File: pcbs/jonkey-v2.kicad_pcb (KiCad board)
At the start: 2 copper layers, 191.3 x 127.7 mm, 149 parts

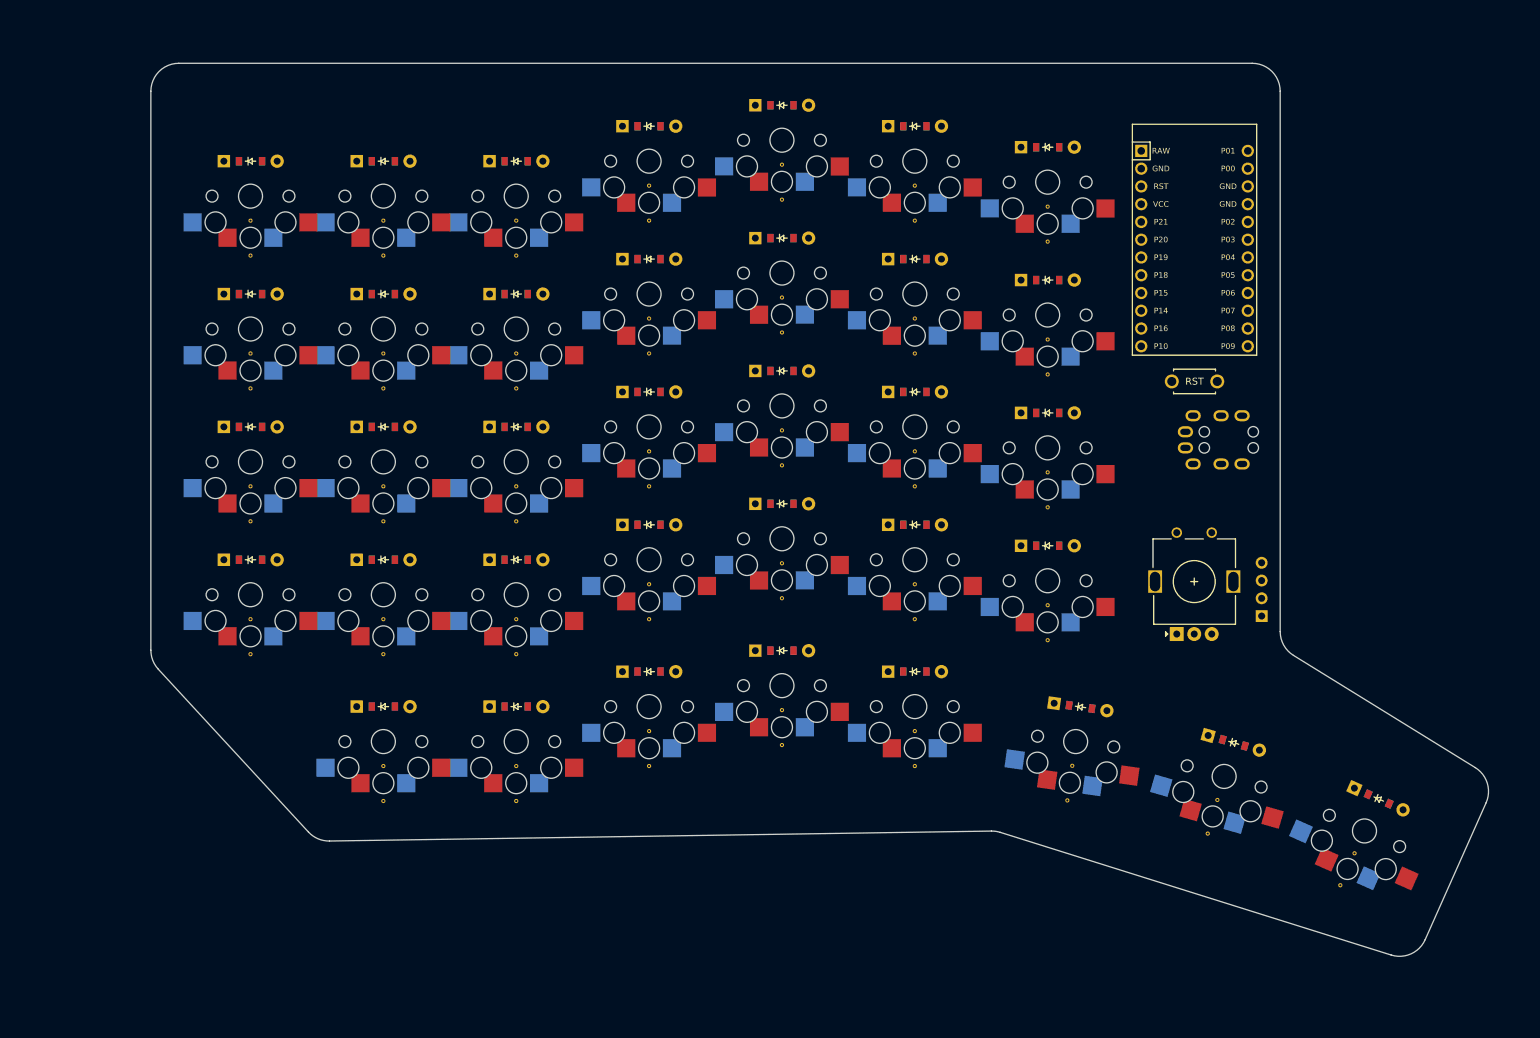
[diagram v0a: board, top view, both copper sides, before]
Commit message: feat: add a few mounting holds, increase thumb distance, increase stagger beyound pinky
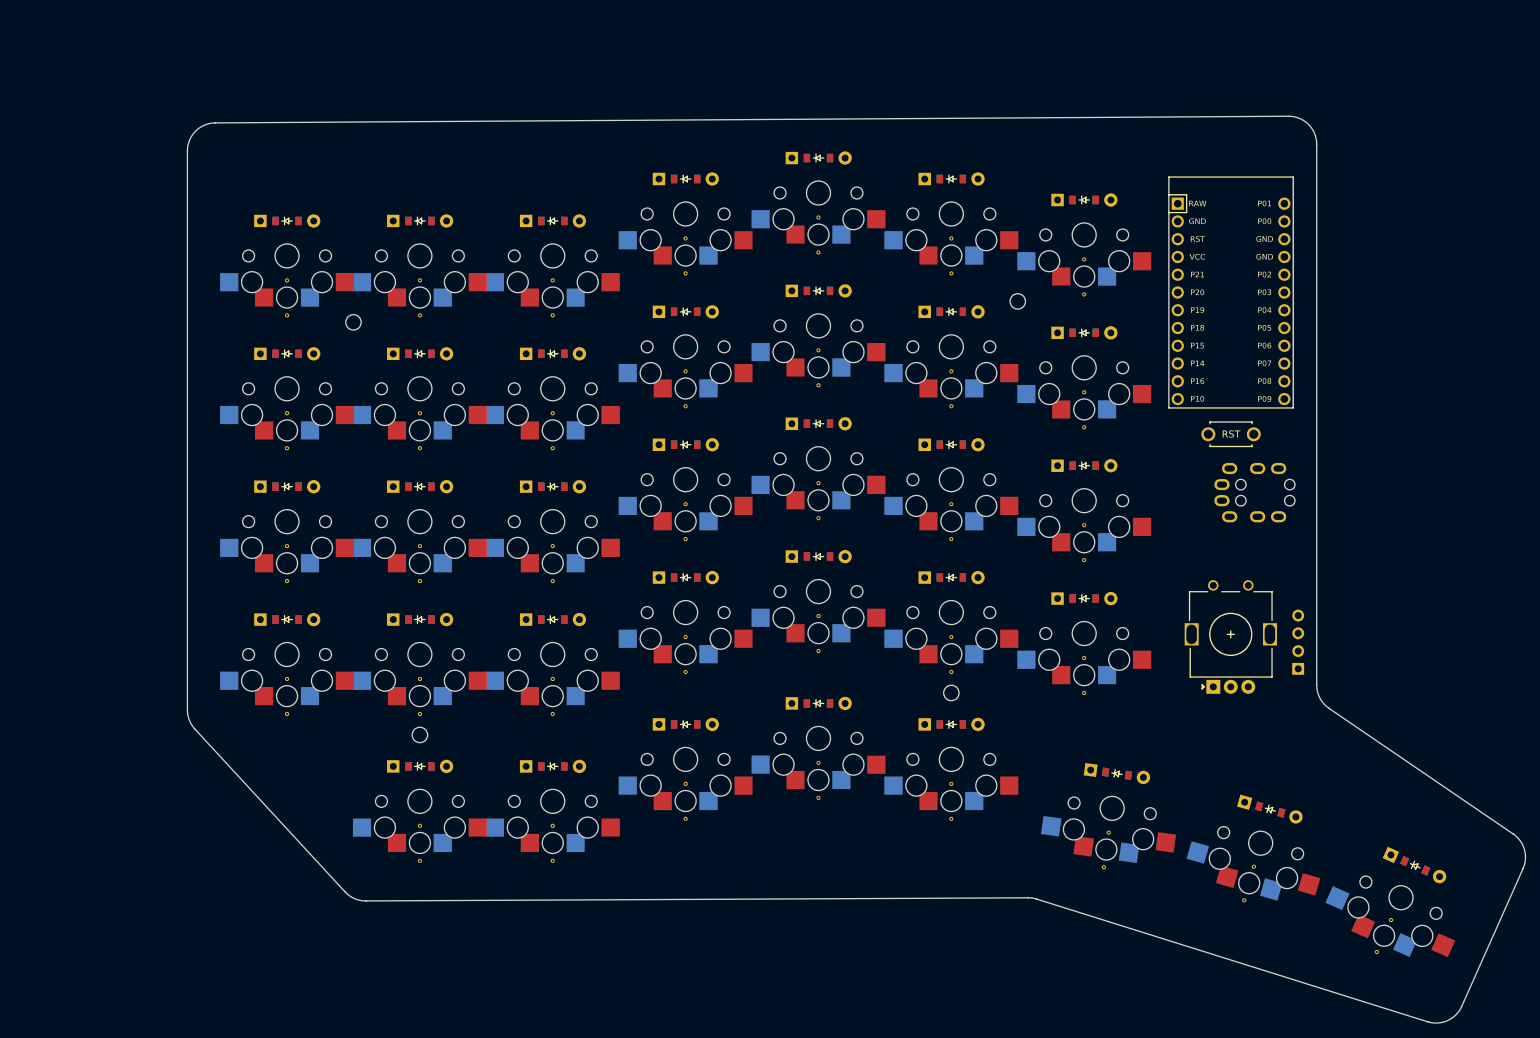
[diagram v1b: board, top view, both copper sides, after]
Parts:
- removed the REF** at (184.0, 158.0)
- removed the REF** at (165.0, 189.0)
- removed the REF** at (244.5, 184.0)
- removed the REF** at (241.0, 109.0)
- removed the REF** at (165.0, 149.0)
- removed the REF** at (127.0, 168.0)
- removed the REF** at (184.0, 125.0)
- removed the REF** at (184.0, 106.0)
- removed the REF** at (127.0, 144.0)
- removed the REF** at (222.0, 158.0)
- removed the REF** at (222.0, 106.0)
- removed the REF** at (146.0, 184.0)
- removed the REF** at (203.0, 122.0)
- removed the REF** at (184.0, 139.0)
- removed the REF** at (222.0, 120.0)
- removed the REF** at (203.0, 136.0)
- removed the REF** at (222.0, 184.0)
- removed the REF** at (165.0, 111.0)
- removed the REF** at (241.0, 128.0)
- removed the REF** at (165.0, 125.0)
- removed the REF** at (146.0, 106.0)
- removed the REF** at (222.0, 144.0)
- removed the REF** at (243.8, 188.9)
- removed the REF** at (203.0, 155.0)
- removed the REF** at (127.0, 111.0)
- removed the REF** at (222.0, 179.0)
- removed the REF** at (165.0, 106.0)
- removed the REF** at (165.0, 163.0)
- removed the REF** at (146.0, 125.0)
- removed the REF** at (127.0, 125.0)
- removed the REF** at (146.0, 163.0)
- removed the REF** at (241.0, 166.0)
- removed the REF** at (203.0, 98.0)
- removed the REF** at (127.0, 163.0)
- removed the REF** at (284.9, 196.5)
- removed the REF** at (222.0, 101.0)
- removed the REF** at (222.0, 163.0)
- removed the REF** at (165.0, 144.0)
- removed the REF** at (241.0, 123.0)
- removed the REF** at (146.0, 149.0)
- removed the REF** at (282.8, 201.0)
- removed the REF** at (241.0, 147.0)
- removed the REF** at (203.0, 141.0)
- removed the REF** at (146.0, 144.0)
- removed the REF** at (165.0, 168.0)
- removed the REF** at (184.0, 101.0)
- removed the REF** at (146.0, 189.0)
- removed the REF** at (146.0, 130.0)
- removed the REF** at (165.0, 184.0)
- removed the REF** at (165.0, 130.0)
- removed the REF** at (184.0, 120.0)
- removed the REF** at (222.0, 125.0)
- removed the REF** at (265.3, 188.8)
- removed the REF** at (127.0, 149.0)
- removed the REF** at (146.0, 168.0)
- removed the REF** at (263.9, 193.7)
- removed the REF** at (184.0, 179.0)
- removed the REF** at (184.0, 144.0)
- removed the REF** at (127.0, 130.0)
- removed the REF** at (241.0, 104.0)
- removed the REF** at (241.0, 161.0)
- removed the REF** at (127.0, 106.0)
- removed the REF** at (184.0, 163.0)
- removed the REF** at (203.0, 103.0)
- removed the REF** at (184.0, 184.0)
- removed the REF** at (203.0, 117.0)
- removed the REF** at (146.0, 111.0)
- removed the REF** at (222.0, 139.0)
- removed the REF** at (203.0, 181.0)
- removed the REF** at (203.0, 176.0)
- removed the REF** at (241.0, 142.0)
- removed the REF** at (203.0, 160.0)
- added MH1: , ceoloide:mounting_hole_npth, F.Cu at (141.7, 120.5)
- added MH2: , ceoloide:mounting_hole_npth, F.Cu at (236.7, 117.5)
- added MH3: , ceoloide:mounting_hole_npth, F.Cu at (151.2, 179.6)
- added MH4: , ceoloide:mounting_hole_npth, F.Cu at (227.2, 173.6)
- added REF**: VIA-0.6mm, VIA-0.6mm, F.Cu at (170.2, 197.6)
- added REF**: VIA-0.6mm, VIA-0.6mm, F.Cu at (189.2, 146.6)
- added REF**: VIA-0.6mm, VIA-0.6mm, F.Cu at (246.2, 173.6)
- added REF**: VIA-0.6mm, VIA-0.6mm, F.Cu at (227.2, 191.6)
- added REF**: VIA-0.6mm, VIA-0.6mm, F.Cu at (151.2, 176.6)
- added REF**: VIA-0.6mm, VIA-0.6mm, F.Cu at (189.2, 127.5)
- added REF**: VIA-0.6mm, VIA-0.6mm, F.Cu at (132.2, 152.6)
- added REF**: VIA-0.6mm, VIA-0.6mm, F.Cu at (189.2, 108.5)
- added REF**: VIA-0.6mm, VIA-0.6mm, F.Cu at (170.2, 119.5)
- added REF**: VIA-0.6mm, VIA-0.6mm, F.Cu at (132.2, 176.6)
- added REF**: VIA-0.6mm, VIA-0.6mm, F.Cu at (170.2, 157.6)
- added REF**: VIA-0.6mm, VIA-0.6mm, F.Cu at (246.2, 168.6)
- added REF**: VIA-0.6mm, VIA-0.6mm, F.Cu at (132.2, 171.6)
- added REF**: VIA-0.6mm, VIA-0.6mm, F.Cu at (151.2, 192.6)
- added REF**: VIA-0.6mm, VIA-0.6mm, F.Cu at (249.7, 193.5)
- added REF**: VIA-0.6mm, VIA-0.6mm, F.Cu at (208.2, 162.6)
- added REF**: VIA-0.6mm, VIA-0.6mm, F.Cu at (132.2, 114.5)
- added REF**: VIA-0.6mm, VIA-0.6mm, F.Cu at (246.2, 111.5)
- added REF**: VIA-0.6mm, VIA-0.6mm, F.Cu at (189.2, 113.5)
- added REF**: VIA-0.6mm, VIA-0.6mm, F.Cu at (208.2, 148.6)
- added REF**: VIA-0.6mm, VIA-0.6mm, F.Cu at (227.2, 132.6)
- added REF**: VIA-0.6mm, VIA-0.6mm, F.Cu at (227.2, 151.6)
- added REF**: VIA-0.6mm, VIA-0.6mm, F.Cu at (227.2, 165.6)
- added REF**: VIA-0.6mm, VIA-0.6mm, F.Cu at (246.2, 149.6)
- added REF**: VIA-0.6mm, VIA-0.6mm, F.Cu at (208.2, 124.5)
- added REF**: VIA-0.6mm, VIA-0.6mm, F.Cu at (208.2, 183.6)
- added REF**: VIA-0.6mm, VIA-0.6mm, F.Cu at (170.2, 176.6)
- added REF**: VIA-0.6mm, VIA-0.6mm, F.Cu at (170.2, 192.6)
- added REF**: VIA-0.6mm, VIA-0.6mm, F.Cu at (189.2, 186.6)
- added REF**: VIA-0.6mm, VIA-0.6mm, F.Cu at (189.2, 170.6)
- added REF**: VIA-0.6mm, VIA-0.6mm, F.Cu at (208.2, 110.5)
- added REF**: VIA-0.6mm, VIA-0.6mm, F.Cu at (227.2, 186.6)
- added REF**: VIA-0.6mm, VIA-0.6mm, F.Cu at (246.2, 154.6)
- added REF**: VIA-0.6mm, VIA-0.6mm, F.Cu at (288.1, 210.6)
- added REF**: VIA-0.6mm, VIA-0.6mm, F.Cu at (208.2, 129.6)
- added REF**: VIA-0.6mm, VIA-0.6mm, F.Cu at (208.2, 188.6)
- added REF**: VIA-0.6mm, VIA-0.6mm, F.Cu at (132.2, 133.6)
- added REF**: VIA-0.6mm, VIA-0.6mm, F.Cu at (227.2, 146.6)
- added REF**: VIA-0.6mm, VIA-0.6mm, F.Cu at (227.2, 113.5)
- added REF**: VIA-0.6mm, VIA-0.6mm, F.Cu at (132.2, 119.5)
- added REF**: VIA-0.6mm, VIA-0.6mm, F.Cu at (170.2, 114.5)
- added REF**: VIA-0.6mm, VIA-0.6mm, F.Cu at (246.2, 130.6)
- added REF**: VIA-0.6mm, VIA-0.6mm, F.Cu at (170.2, 138.6)
- added REF**: VIA-0.6mm, VIA-0.6mm, F.Cu at (227.2, 108.5)
- added REF**: VIA-0.6mm, VIA-0.6mm, F.Cu at (170.2, 152.6)
- added REF**: VIA-0.6mm, VIA-0.6mm, F.Cu at (132.2, 157.6)
- added REF**: VIA-0.6mm, VIA-0.6mm, F.Cu at (132.2, 138.6)
- added REF**: VIA-0.6mm, VIA-0.6mm, F.Cu at (151.2, 197.6)
- added REF**: VIA-0.6mm, VIA-0.6mm, F.Cu at (227.2, 170.6)
- added REF**: VIA-0.6mm, VIA-0.6mm, F.Cu at (189.2, 151.6)
- added REF**: VIA-0.6mm, VIA-0.6mm, F.Cu at (151.2, 119.5)
- added REF**: VIA-0.6mm, VIA-0.6mm, F.Cu at (151.2, 157.6)
- added REF**: VIA-0.6mm, VIA-0.6mm, F.Cu at (189.2, 165.6)
- added REF**: VIA-0.6mm, VIA-0.6mm, F.Cu at (270.5, 198.4)
- added REF**: VIA-0.6mm, VIA-0.6mm, F.Cu at (151.2, 114.5)
- added REF**: VIA-0.6mm, VIA-0.6mm, F.Cu at (208.2, 143.6)
- added REF**: VIA-0.6mm, VIA-0.6mm, F.Cu at (151.2, 138.6)
- added REF**: VIA-0.6mm, VIA-0.6mm, F.Cu at (269.1, 203.2)
- added REF**: VIA-0.6mm, VIA-0.6mm, F.Cu at (227.2, 127.5)
- added REF**: VIA-0.6mm, VIA-0.6mm, F.Cu at (170.2, 133.6)
- added REF**: VIA-0.6mm, VIA-0.6mm, F.Cu at (189.2, 191.6)
- added REF**: VIA-0.6mm, VIA-0.6mm, F.Cu at (151.2, 171.6)
- added REF**: VIA-0.6mm, VIA-0.6mm, F.Cu at (246.2, 116.5)
- added REF**: VIA-0.6mm, VIA-0.6mm, F.Cu at (170.2, 171.6)
- added REF**: VIA-0.6mm, VIA-0.6mm, F.Cu at (189.2, 132.6)
- added REF**: VIA-0.6mm, VIA-0.6mm, F.Cu at (151.2, 133.6)
- added REF**: VIA-0.6mm, VIA-0.6mm, F.Cu at (208.2, 105.5)
- added REF**: VIA-0.6mm, VIA-0.6mm, F.Cu at (246.2, 135.6)
- added REF**: VIA-0.6mm, VIA-0.6mm, F.Cu at (208.2, 167.6)
- added REF**: VIA-0.6mm, VIA-0.6mm, F.Cu at (151.2, 152.6)
- added REF**: VIA-0.6mm, VIA-0.6mm, F.Cu at (249.0, 198.5)
- added REF**: VIA-0.6mm, VIA-0.6mm, F.Cu at (290.1, 206.0)
- moved S35 10.9 mm to (271.5, 195.0)
- moved S34 10.9 mm to (250.2, 190.1)
- moved D35 10.9 mm to (272.8, 190.2)
- moved S36 10.9 mm to (291.5, 202.8)
- moved D34 10.9 mm to (250.9, 185.1)
- moved D36 10.9 mm to (293.6, 198.3)
- moved D1 10.0 mm to (132.2, 163.1)
- moved D10 10.0 mm to (170.2, 184.1)
- moved D11 10.0 mm to (170.2, 163.1)
- moved D12 10.0 mm to (170.2, 144.1)
- moved D2 10.0 mm to (132.2, 144.1)
- moved D5 10.0 mm to (151.2, 184.1)
- moved D6 10.0 mm to (151.2, 163.1)
- moved D7 10.0 mm to (151.2, 144.1)
- moved S1 10.0 mm to (132.2, 168.1)
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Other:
- board size 191.3 x 127.7 mm -> 191.4 x 129.7 mm

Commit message: feat: add place for pull up resistors for i2c
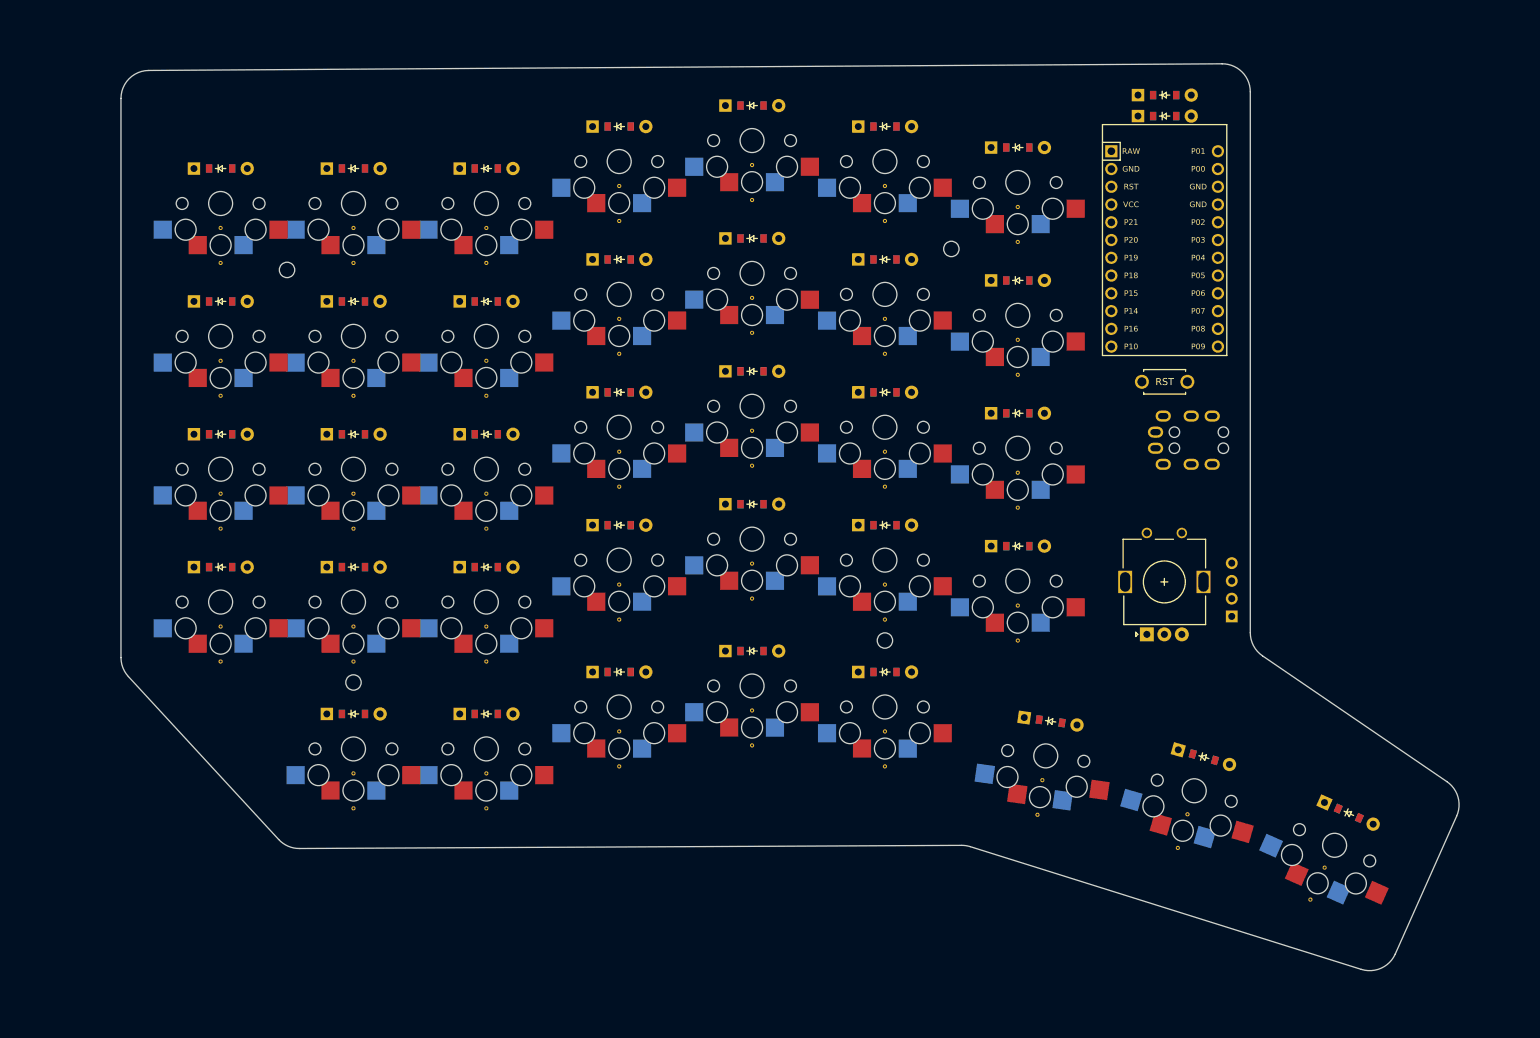
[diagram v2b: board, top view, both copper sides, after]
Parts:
- removed the REF** at (170.2, 197.6)
- removed the REF** at (189.2, 146.6)
- removed the REF** at (246.2, 173.6)
- removed the REF** at (227.2, 191.6)
- removed the REF** at (151.2, 176.6)
- removed the REF** at (189.2, 127.5)
- removed the REF** at (132.2, 152.6)
- removed the REF** at (189.2, 108.5)
- removed the REF** at (170.2, 119.5)
- removed the REF** at (132.2, 176.6)
- removed the REF** at (170.2, 157.6)
- removed the REF** at (246.2, 168.6)
- removed the REF** at (132.2, 171.6)
- removed the REF** at (151.2, 192.6)
- removed the REF** at (249.7, 193.5)
- removed the REF** at (208.2, 162.6)
- removed the REF** at (132.2, 114.5)
- removed the REF** at (246.2, 111.5)
- removed the REF** at (189.2, 113.5)
- removed the REF** at (208.2, 148.6)
- removed the REF** at (227.2, 132.6)
- removed the REF** at (227.2, 151.6)
- removed the REF** at (227.2, 165.6)
- removed the REF** at (246.2, 149.6)
- removed the REF** at (208.2, 124.5)
- removed the REF** at (208.2, 183.6)
- removed the REF** at (170.2, 176.6)
- removed the REF** at (170.2, 192.6)
- removed the REF** at (189.2, 186.6)
- removed the REF** at (189.2, 170.6)
- removed the REF** at (208.2, 110.5)
- removed the REF** at (227.2, 186.6)
- removed the REF** at (246.2, 154.6)
- removed the REF** at (288.1, 210.6)
- removed the REF** at (208.2, 129.6)
- removed the REF** at (208.2, 188.6)
- removed the REF** at (132.2, 133.6)
- removed the REF** at (227.2, 146.6)
- removed the REF** at (227.2, 113.5)
- removed the REF** at (132.2, 119.5)
- removed the REF** at (170.2, 114.5)
- removed the REF** at (246.2, 130.6)
- removed the REF** at (170.2, 138.6)
- removed the REF** at (227.2, 108.5)
- removed the REF** at (170.2, 152.6)
- removed the REF** at (132.2, 157.6)
- removed the REF** at (132.2, 138.6)
- removed the REF** at (151.2, 197.6)
- removed the REF** at (227.2, 170.6)
- removed the REF** at (189.2, 151.6)
- removed the REF** at (151.2, 119.5)
- removed the REF** at (151.2, 157.6)
- removed the REF** at (189.2, 165.6)
- removed the REF** at (270.5, 198.4)
- removed the REF** at (151.2, 114.5)
- removed the REF** at (208.2, 143.6)
- removed the REF** at (151.2, 138.6)
- removed the REF** at (269.1, 203.2)
- removed the REF** at (227.2, 127.5)
- removed the REF** at (170.2, 133.6)
- removed the REF** at (189.2, 191.6)
- removed the REF** at (151.2, 171.6)
- removed the REF** at (246.2, 116.5)
- removed the REF** at (170.2, 171.6)
- removed the REF** at (189.2, 132.6)
- removed the REF** at (151.2, 133.6)
- removed the REF** at (208.2, 105.5)
- removed the REF** at (246.2, 135.6)
- removed the REF** at (208.2, 167.6)
- removed the REF** at (151.2, 152.6)
- removed the REF** at (249.0, 198.5)
- removed the REF** at (290.1, 206.0)
- added R11: , ComboDiode, F.Cu at (257.7, 88.0)
- added R21: , ComboDiode, F.Cu at (257.7, 91.0)
- added REF**: VIA-0.6mm, VIA-0.6mm, F.Cu at (239.5, 191.0)
- added REF**: VIA-0.6mm, VIA-0.6mm, F.Cu at (179.7, 139.1)
- added REF**: VIA-0.6mm, VIA-0.6mm, F.Cu at (259.6, 195.7)
- added REF**: VIA-0.6mm, VIA-0.6mm, F.Cu at (236.7, 147.1)
- added REF**: VIA-0.6mm, VIA-0.6mm, F.Cu at (179.7, 184.1)
- added REF**: VIA-0.6mm, VIA-0.6mm, F.Cu at (280.6, 198.5)
- added REF**: VIA-0.6mm, VIA-0.6mm, F.Cu at (236.7, 109.0)
- added REF**: VIA-0.6mm, VIA-0.6mm, F.Cu at (160.7, 131.1)
- added REF**: VIA-0.6mm, VIA-0.6mm, F.Cu at (141.7, 107.0)
- added REF**: VIA-0.6mm, VIA-0.6mm, F.Cu at (160.7, 169.1)
- added REF**: VIA-0.6mm, VIA-0.6mm, F.Cu at (160.7, 126.0)
- added REF**: VIA-0.6mm, VIA-0.6mm, F.Cu at (179.7, 101.0)
- added REF**: VIA-0.6mm, VIA-0.6mm, F.Cu at (122.7, 164.1)
- added REF**: VIA-0.6mm, VIA-0.6mm, F.Cu at (198.7, 181.1)
- added REF**: VIA-0.6mm, VIA-0.6mm, F.Cu at (217.7, 139.1)
- added REF**: VIA-0.6mm, VIA-0.6mm, F.Cu at (179.7, 144.1)
- added REF**: VIA-0.6mm, VIA-0.6mm, F.Cu at (122.7, 145.1)
- added REF**: VIA-0.6mm, VIA-0.6mm, F.Cu at (179.7, 163.1)
- added REF**: VIA-0.6mm, VIA-0.6mm, F.Cu at (217.7, 101.0)
- added REF**: VIA-0.6mm, VIA-0.6mm, F.Cu at (198.7, 155.1)
- added REF**: VIA-0.6mm, VIA-0.6mm, F.Cu at (198.7, 176.1)
- added REF**: VIA-0.6mm, VIA-0.6mm, F.Cu at (217.7, 120.0)
- added REF**: VIA-0.6mm, VIA-0.6mm, F.Cu at (122.7, 107.0)
- added REF**: VIA-0.6mm, VIA-0.6mm, F.Cu at (217.7, 125.0)
- added REF**: VIA-0.6mm, VIA-0.6mm, F.Cu at (261.0, 190.9)
- added REF**: VIA-0.6mm, VIA-0.6mm, F.Cu at (141.7, 164.1)
- added REF**: VIA-0.6mm, VIA-0.6mm, F.Cu at (240.2, 186.0)
- added REF**: VIA-0.6mm, VIA-0.6mm, F.Cu at (198.7, 117.0)
- added REF**: VIA-0.6mm, VIA-0.6mm, F.Cu at (179.7, 158.1)
- added REF**: VIA-0.6mm, VIA-0.6mm, F.Cu at (198.7, 98.0)
- added REF**: VIA-0.6mm, VIA-0.6mm, F.Cu at (160.7, 145.1)
- added REF**: VIA-0.6mm, VIA-0.6mm, F.Cu at (141.7, 150.1)
- added REF**: VIA-0.6mm, VIA-0.6mm, F.Cu at (198.7, 136.1)
- added REF**: VIA-0.6mm, VIA-0.6mm, F.Cu at (236.7, 104.0)
- added REF**: VIA-0.6mm, VIA-0.6mm, F.Cu at (217.7, 144.1)
- added REF**: VIA-0.6mm, VIA-0.6mm, F.Cu at (141.7, 131.1)
- added REF**: VIA-0.6mm, VIA-0.6mm, F.Cu at (179.7, 179.1)
- added REF**: VIA-0.6mm, VIA-0.6mm, F.Cu at (179.7, 120.0)
- added REF**: VIA-0.6mm, VIA-0.6mm, F.Cu at (141.7, 185.1)
- added REF**: VIA-0.6mm, VIA-0.6mm, F.Cu at (278.6, 203.1)
- added REF**: VIA-0.6mm, VIA-0.6mm, F.Cu at (122.7, 150.1)
- added REF**: VIA-0.6mm, VIA-0.6mm, F.Cu at (217.7, 163.1)
- added REF**: VIA-0.6mm, VIA-0.6mm, F.Cu at (198.7, 160.1)
- added REF**: VIA-0.6mm, VIA-0.6mm, F.Cu at (141.7, 190.1)
- added REF**: VIA-0.6mm, VIA-0.6mm, F.Cu at (198.7, 141.1)
- added REF**: VIA-0.6mm, VIA-0.6mm, F.Cu at (122.7, 169.1)
- added REF**: VIA-0.6mm, VIA-0.6mm, F.Cu at (122.7, 131.1)
- added REF**: VIA-0.6mm, VIA-0.6mm, F.Cu at (122.7, 112.0)
- added REF**: VIA-0.6mm, VIA-0.6mm, F.Cu at (236.7, 161.1)
- added REF**: VIA-0.6mm, VIA-0.6mm, F.Cu at (141.7, 169.1)
- added REF**: VIA-0.6mm, VIA-0.6mm, F.Cu at (179.7, 106.0)
- added REF**: VIA-0.6mm, VIA-0.6mm, F.Cu at (217.7, 179.1)
- added REF**: VIA-0.6mm, VIA-0.6mm, F.Cu at (160.7, 107.0)
- added REF**: VIA-0.6mm, VIA-0.6mm, F.Cu at (236.7, 128.1)
- added REF**: VIA-0.6mm, VIA-0.6mm, F.Cu at (217.7, 106.0)
- added REF**: VIA-0.6mm, VIA-0.6mm, F.Cu at (217.7, 184.1)
- added REF**: VIA-0.6mm, VIA-0.6mm, F.Cu at (179.7, 125.0)
- added REF**: VIA-0.6mm, VIA-0.6mm, F.Cu at (141.7, 145.1)
- added REF**: VIA-0.6mm, VIA-0.6mm, F.Cu at (236.7, 166.1)
- added REF**: VIA-0.6mm, VIA-0.6mm, F.Cu at (198.7, 122.0)
- added REF**: VIA-0.6mm, VIA-0.6mm, F.Cu at (141.7, 126.0)
- added REF**: VIA-0.6mm, VIA-0.6mm, F.Cu at (236.7, 142.1)
- added REF**: VIA-0.6mm, VIA-0.6mm, F.Cu at (122.7, 126.0)
- added REF**: VIA-0.6mm, VIA-0.6mm, F.Cu at (160.7, 164.1)
- added REF**: VIA-0.6mm, VIA-0.6mm, F.Cu at (160.7, 112.0)
- added REF**: VIA-0.6mm, VIA-0.6mm, F.Cu at (198.7, 103.0)
- added REF**: VIA-0.6mm, VIA-0.6mm, F.Cu at (236.7, 123.0)
- added REF**: VIA-0.6mm, VIA-0.6mm, F.Cu at (141.7, 112.0)
- added REF**: VIA-0.6mm, VIA-0.6mm, F.Cu at (160.7, 150.1)
- added REF**: VIA-0.6mm, VIA-0.6mm, F.Cu at (217.7, 158.1)
- added REF**: VIA-0.6mm, VIA-0.6mm, F.Cu at (160.7, 190.1)
- added REF**: VIA-0.6mm, VIA-0.6mm, F.Cu at (160.7, 185.1)
- moved D22 12.1 mm to (198.7, 127.5)
- moved S13 12.1 mm to (160.7, 122.5)
- moved S3 12.1 mm to (122.7, 122.5)
- moved S8 12.1 mm to (141.7, 122.5)
- moved D1 12.1 mm to (122.7, 155.6)
- moved D10 12.1 mm to (160.7, 176.6)
- moved D11 12.1 mm to (160.7, 155.6)
- moved D12 12.1 mm to (160.7, 136.6)
- moved D13 12.1 mm to (160.7, 117.5)
- moved D14 12.1 mm to (160.7, 98.5)
- moved D15 12.1 mm to (179.7, 170.6)
- moved D16 12.1 mm to (179.7, 149.6)
- moved D17 12.1 mm to (179.7, 130.6)
- moved D18 12.1 mm to (179.7, 111.5)
- moved D19 12.1 mm to (179.7, 92.5)
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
